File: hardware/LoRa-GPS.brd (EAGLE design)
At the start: 50.8 x 17.8 mm, 27 parts, among them J2 MF-CON-MICROUSB-RIGHT, U1 MCP1703-3302E/CB, Y1 CRYSTAL.ABS07

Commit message: lipo
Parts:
- added C10: 4.7uF, SparkFun-Capacitors:0603
- added C11: 10uF, SparkFun-Capacitors:EIA3216
- added D4: BLUE, SparkFun-LED:LED-0603
- added J8: (no value), SparkFun-Connectors:1X02_NO_SILK
- added R5: 2.0k, SparkFun-Resistors:0603
- added R9: 1k, SparkFun-Resistors:0603
- added U2: MCP73831, SparkFun-IC-Power:SOT23-5
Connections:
- new net CHARGE_STAT: R9.1, U2.1
- new net N$11: R5.1, U2.5
- new net N$8: D4.C, R9.2
- new net V_BATT: C11.+, U2.3
- new net V_USB: C10.1, D4.A, J8.2, U2.4
- net GND: now also C10.2, C11.-, J8.1, R5.2, U2.2
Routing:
- net VIN: track 13.1 -> 11.5 mm

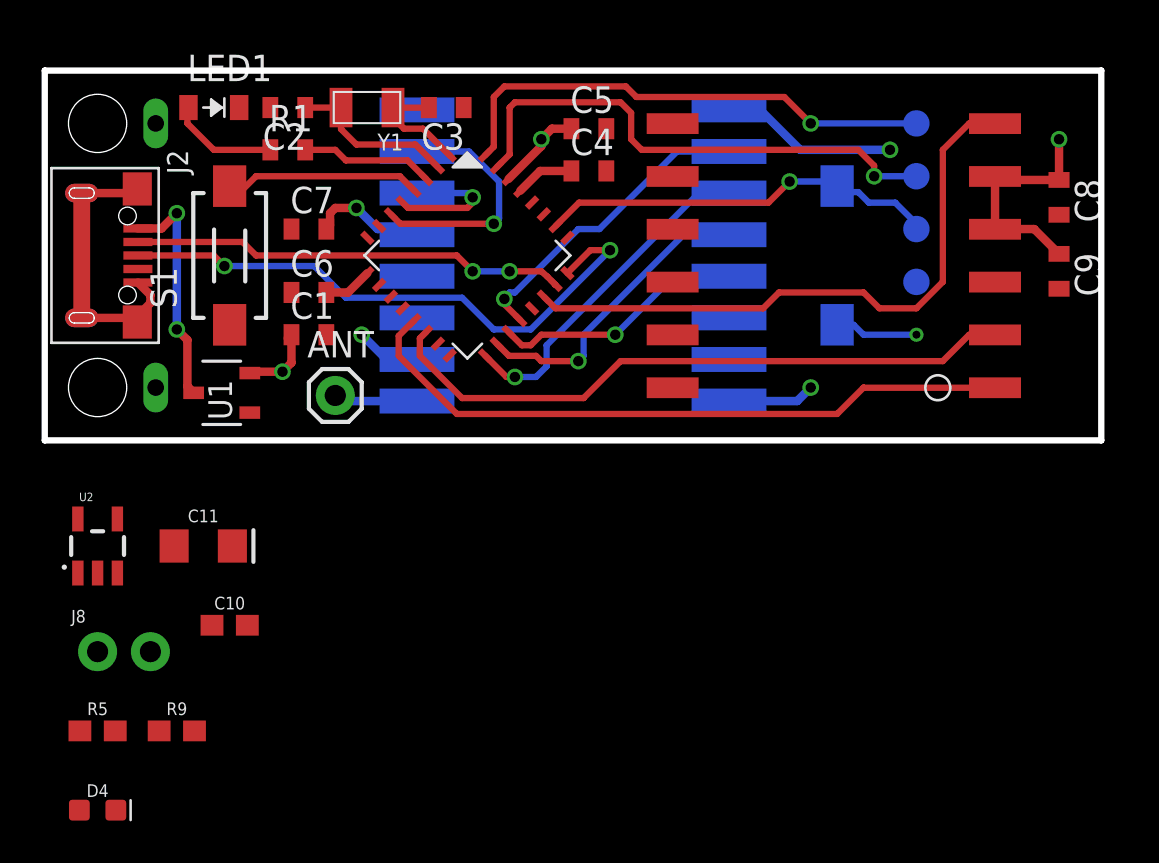
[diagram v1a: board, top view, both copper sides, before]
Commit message: remove DRC warnings
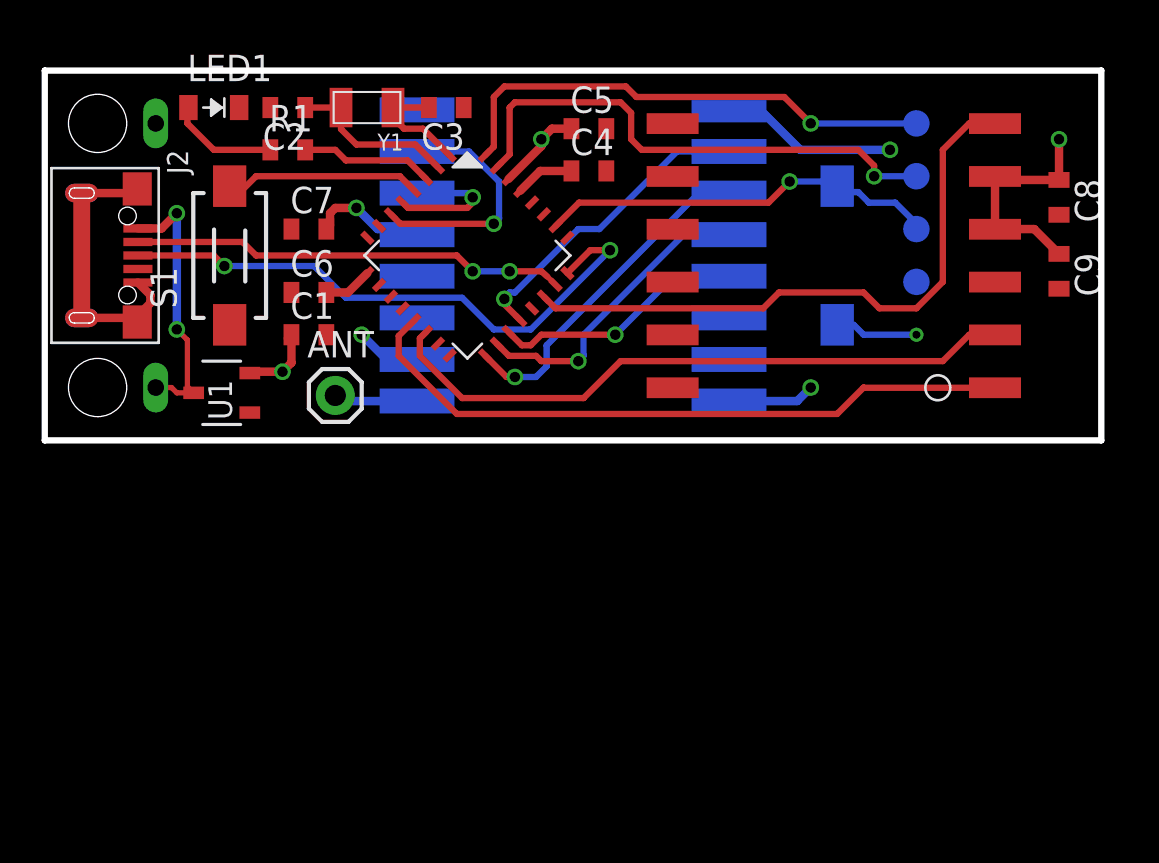
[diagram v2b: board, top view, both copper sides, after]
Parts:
- removed C10: 4.7uF, SparkFun-Capacitors:0603
- removed C11: 10uF, SparkFun-Capacitors:EIA3216
- removed D4: BLUE, SparkFun-LED:LED-0603
- removed J8: (no value), SparkFun-Connectors:1X02_NO_SILK
- removed R5: 2.0k, SparkFun-Resistors:0603
- removed R9: 1k, SparkFun-Resistors:0603
- removed U2: MCP73831, SparkFun-IC-Power:SOT23-5
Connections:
- removed net CHARGE_STAT: R9.1, U2.1
- removed net N$11: R5.1, U2.5
- removed net N$8: D4.C, R9.2
- removed net V_BATT: C11.+, U2.3
- removed net V_USB: C10.1, D4.A, J8.2, U2.4
- net GND: no longer C10.2, C11.-, J8.1, R5.2, U2.2
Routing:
- net VIN: track 11.5 -> 13.1 mm
- net N$3: track 9.04 -> 8.42 mm

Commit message: remove switch move TP's
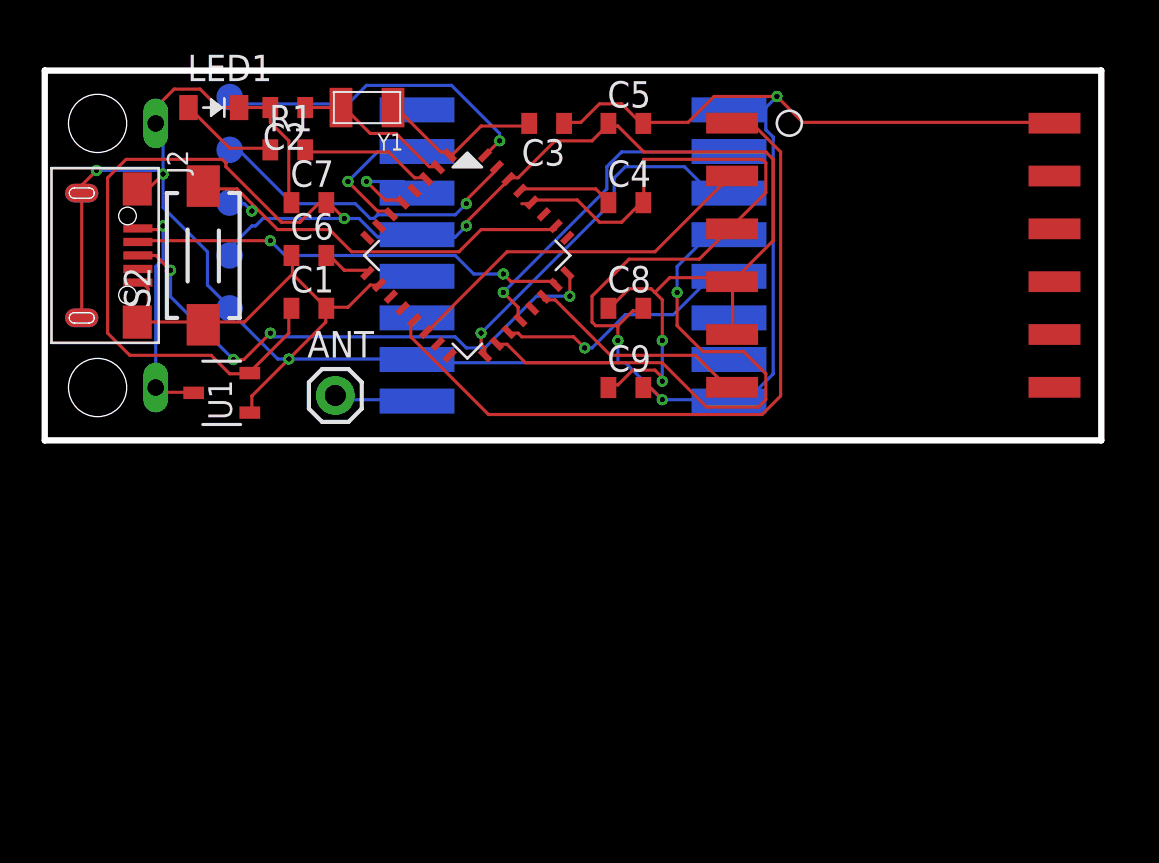
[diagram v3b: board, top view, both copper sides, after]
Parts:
- removed S1: DTSM-3, switch-tact:DTSM-3
- TP1: device SparkFun-Passives:TP_15TH -> SparkFun-Passives:PAD.03X.05
- moved TP1 33.0 mm to (8.89, 6.35), flipped to the bottom, turned to 180 degrees
- moved TP2 33.0 mm to (8.89, 8.89)
- moved TP3 33.0 mm to (8.89, 11.4)
- moved TP4 33.0 mm to (8.89, 14.0)
- moved TP5 33.0 mm to (8.89, 16.5)
- moved GPS 30.6 mm to (50.8, 19.1), turned to 180 degrees
- moved S2 30.5 mm to (7.62, 8.89), flipped to the top
- moved C9 21.6 mm to (27.9, 2.54), turned to 0 degrees
- moved C8 21.5 mm to (27.9, 6.35), turned to 0 degrees
- moved C3 4.89 mm to (24.1, 15.2)
- moved C4 2.34 mm to (27.9, 11.4)
- moved C5 1.80 mm to (27.9, 15.2)
- moved C6 1.78 mm to (12.7, 8.89)
- moved C1 1.27 mm to (12.7, 6.35)
- moved C7 1.27 mm to (12.7, 11.4)
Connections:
- removed net N$9: S1.2, SAMD21.4
- net GND: no longer S1.1
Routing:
- net GND: track 33.8 -> 164.7 mm, vias 3 -> 6
- net VCC: track 25.4 -> 87.2 mm
- net D21: track 30.0 -> 11.0 mm
- net RX: track 31.0 -> 17.8 mm
- net SCK: track 14.6 -> 26.8 mm
- net N$9: track 10.1 -> 0.00 mm
- net SWCLK: track 25.3 -> 15.4 mm
- net SWDIO: track 24.3 -> 15.9 mm
- net D18: track 11.8 -> 6.64 mm
- net TX: track 32.4 -> 35.3 mm
- net VIN: track 13.1 -> 11.2 mm, vias 2 -> 1
- net D17: track 6.59 -> 4.81 mm
- net N$5: track 2.85 -> 4.57 mm
- net D+: track 28.3 -> 26.6 mm, vias 2 -> 4
- net MOSI: track 16.4 -> 17.5 mm
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- added copper zone on layer 16, net GND
- removed copper zone on layer 16, net VCC

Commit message: tidy
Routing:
- net GND: track 164.7 -> 164.0 mm
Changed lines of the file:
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@@
 <drawing>
 <settings>
-<setting alwaysvectorfont="yes"/>
+<setting alwaysvectorfont="no"/>
 <setting keepoldvectorfont="yes"/>
 <setting verticaltext="up"/>
@@
 <layer number="23" name="tOrigins" color="15" fill="1" visible="yes" active="yes"/>
 <layer number="24" name="bOrigins" color="15" fill="1" visible="yes" active="yes"/>
-<layer number="25" name="tNames" color="7" fill="1" visible="yes" active="yes"/>
-<layer number="26" name="bNames" color="7" fill="1" visible="yes" active="yes"/>
+<layer number="25" name="tNames" color="7" fill="1" visible="no" active="yes"/>
+<layer number="26" name="bNames" color="7" fill="1" visible="no" active="yes"/>
 <layer number="27" name="tValues" color="7" fill="1" visible="no" active="yes"/>
 <layer number="28" name="bValues" color="7" fill="1" visible="no" active="yes"/>
@@
 <layer number="37" name="tTest" color="7" fill="1" visible="no" active="yes"/>
 <layer number="38" name="bTest" color="7" fill="1" visible="no" active="yes"/>
-<layer number="39" name="tKeepout" color="4" fill="11" visible="yes" active="yes"/>
-<layer number="40" name="bKeepout" color="1" fill="11" visible="yes" active="yes"/>
-<layer number="41" name="tRestrict" color="4" fill="10" visible="yes" active="yes"/>
-<layer number="42" name="bRestrict" color="1" fill="10" visible="yes" active="yes"/>
+<layer number="39" name="tKeepout" color="4" fill="11" visible="no" active="yes"/>
+<layer number="40" name="bKeepout" color="1" fill="11" visible="no" active="yes"/>
+<layer number="41" name="tRestrict" color="4" fill="10" visible="no" active="yes"/>
+<layer number="42" name="bRestrict" color="1" fill="10" visible="no" active="yes"/>
 <layer number="43" name="vRestrict" color="2" fill="10" visible="no" active="yes"/>
 <layer number="44" name="Drills" color="7" fill="1" visible="no" active="yes"/>
-<layer number="45" name="Holes" color="7" fill="1" visible="no" active="yes"/>
+<layer number="45" name="Holes" color="7" fill="1" visible="yes" active="yes"/>
 <layer number="46" name="Milling" color="3" fill="1" visible="no" active="yes"/>
 <layer number="47" name="Measures" color="7" fill="1" visible="no" active="yes"/>
@@
 <layer number="50" name="dxf" color="7" fill="1" visible="no" active="no"/>
 <layer number="51" name="tDocu" color="6" fill="1" visible="yes" active="yes"/>
-<layer number="52" name="bDocu" color="7" fill="1" visible="yes" active="yes"/>
+<layer number="52" name="bDocu" color="7" fill="1" visible="no" active="yes"/>
 <layer number="53" name="tGND_GNDA" color="7" fill="9" visible="no" active="no"/>
 <layer number="54" name="bGND_GNDA" color="1" fill="9" visible="no" active="no"/>
@@
 <contactref element="C1" pad="2"/>
 <contactref element="C4" pad="2"/>
-<contactref element="SAMD21" pad="28"/>
 <contactref element="C5" pad="2"/>
 <contactref element="J2" pad="5"/>
@@
 <wire x1="27.7368" y1="10.4902" x2="26.67" y2="10.4902" width="0.1524" layer="1"/>
 <wire x1="28.6258" y1="11.3792" x2="27.7368" y2="10.4902" width="0.1524" layer="1"/>
-<wire x1="23.4696" y1="11.557" x2="23.43126875" y2="11.435584375" width="0.1524" layer="1"/>
 <wire x1="28.6258" y1="11.3792" x2="28.7782" y2="11.43" width="0.1524" layer="1"/>
 <wire x1="28.8036" y1="11.557" x2="28.8036" y2="13.5128" width="0.1524" layer="1"/>
@@
 <wire x1="9.779" y1="1.4224" x2="9.859" y2="1.336" width="0.1524" layer="1"/>
 <wire x1="7.6454" y1="5.5118" x2="7.62" y2="5.555" width="0.1524" layer="1"/>
-<wire x1="22.9362" y1="11.3792" x2="23.2918" y2="11.3792" width="0.1524" layer="1"/>
-<wire x1="23.2918" y1="11.3792" x2="23.43126875" y2="11.435584375" width="0.1524" layer="1"/>
 <wire x1="16.1798" y1="7.6454" x2="16.07735625" y2="7.475784375" width="0.1524" layer="1"/>
 <wire x1="34.671" y1="11.9126" x2="33.0708" y2="10.3124" width="0.1524" layer="1"/>
@@
 <vertex x="50.8" y="17.78"/>
 </polygon>
+<contactref element="SAMD21" pad="28"/>
 </signal>
 <signal name="VCC">
 <contactref element="C1" pad="1"/>
 <contactref element="U1" pad="2"/>
-<contactref element="SAMD21" pad="30"/>
 <contactref element="C5" pad="1"/>
 <contactref element="RADIO" pad="B4"/>
@@
 <wire x1="26.3144" y1="14.4018" x2="24.5364" y2="14.4018" width="0.1524" layer="1"/>
 <wire x1="27.0256" y1="15.113" x2="26.3144" y2="14.4018" width="0.1524" layer="1"/>
-<wire x1="22.4028" y1="12.6238" x2="22.299896875" y2="12.566953125" width="0.1524" layer="1"/>
 <wire x1="27.0256" y1="15.113" x2="27.1018" y2="15.24" width="0.1524" layer="1"/>
 <wire x1="27.559" y1="2.667" x2="27.2034" y2="2.667" width="0.1524" layer="1"/>
@@
 <wire x1="19.7358" y1="9.779" x2="20.2692" y2="10.3124" width="0.1524" layer="16"/>
 <wire x1="17.9578" y1="9.779" x2="19.7358" y2="9.779" width="0.1524" layer="16"/>
-<wire x1="22.225" y1="12.446" x2="22.299896875" y2="12.566953125" width="0.1524" layer="1"/>
 <wire x1="17.9578" y1="9.779" x2="17.9" y2="9.89" width="0.1524" layer="16"/>
 <via x="29.6926" y="2.8448" extent="1-16" drill="0.254"/>
@@
 <via x="14.4018" y="10.668" extent="1-16" drill="0.254"/>
 <via x="20.2692" y="10.3124" extent="1-16" drill="0.254"/>
-</signal>
-<signal name="N$5">
-<contactref element="SAMD21" pad="29"/>
-<contactref element="C4" pad="1"/>
-<wire x1="26.4922" y1="12.0904" x2="22.9362" y2="12.0904" width="0.1524" layer="1"/>
-<wire x1="27.0256" y1="11.557" x2="26.4922" y2="12.0904" width="0.1524" layer="1"/>
-<wire x1="22.9362" y1="12.0904" x2="22.865584375" y2="12.00126875" width="0.1524" layer="1"/>
-<wire x1="27.0256" y1="11.557" x2="27.1018" y2="11.43" width="0.1524" layer="1"/>
+<contactref element="SAMD21" pad="30"/>
+<wire x1="22.4028" y1="12.6238" x2="22.299896875" y2="12.566953125" width="0.1524" layer="1"/>
+<wire x1="22.225" y1="12.446" x2="22.299896875" y2="12.566953125" width="0.1524" layer="1"/>
 </signal>
 <signal name="VIN">
@@
 <signal name="N$10">
 </signal>
+<signal name="N$5">
+<contactref element="SAMD21" pad="29"/>
+<contactref element="C4" pad="1"/>
+<wire x1="22.865584375" y1="12.00126875" x2="23.564315625" y2="12.7" width="0.1524" layer="1"/>
+<wire x1="25.8318" y1="12.7" x2="27.1018" y2="11.43" width="0.1524" layer="1"/>
+<wire x1="23.564315625" y1="12.7" x2="25.8318" y2="12.7" width="0.1524" layer="1"/>
+</signal>
 </signals>

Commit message: tinker
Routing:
- net GND: track 164.0 -> 36.2 mm, vias 6 -> 5

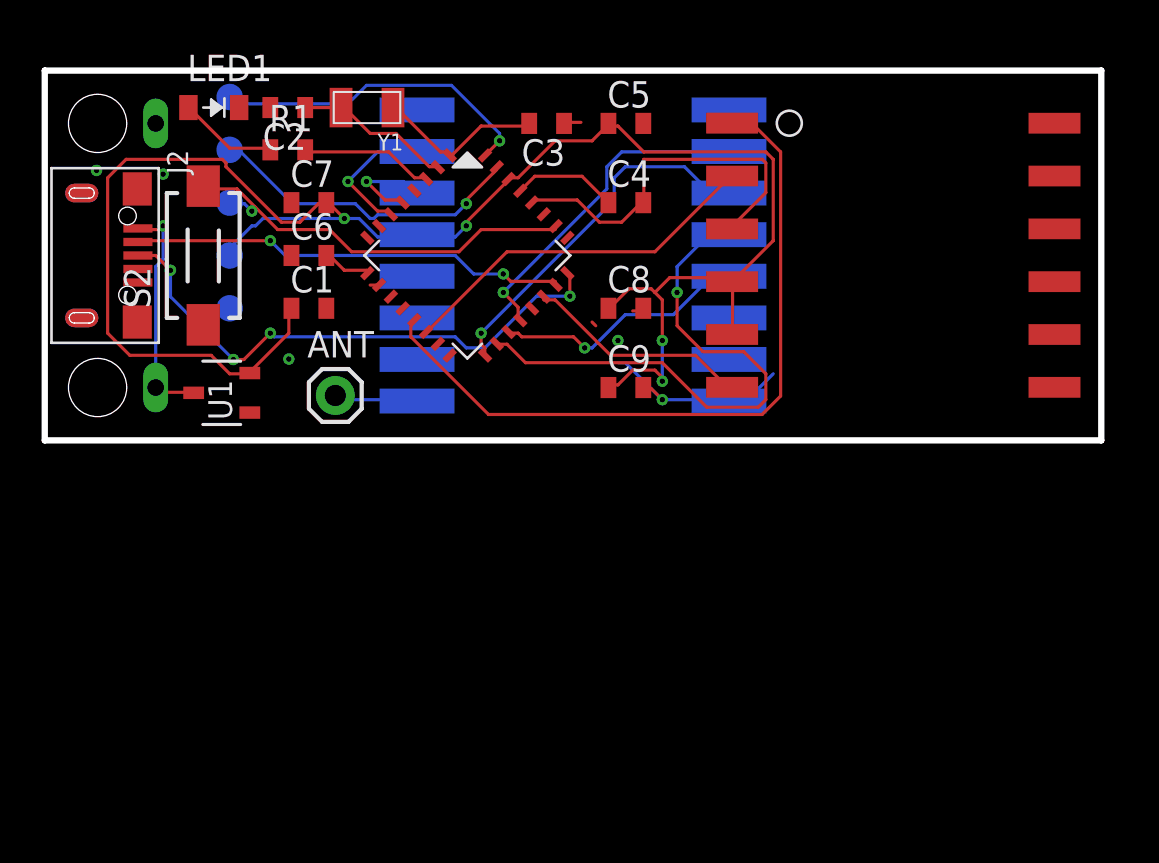
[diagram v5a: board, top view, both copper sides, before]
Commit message: RF and GPS underside
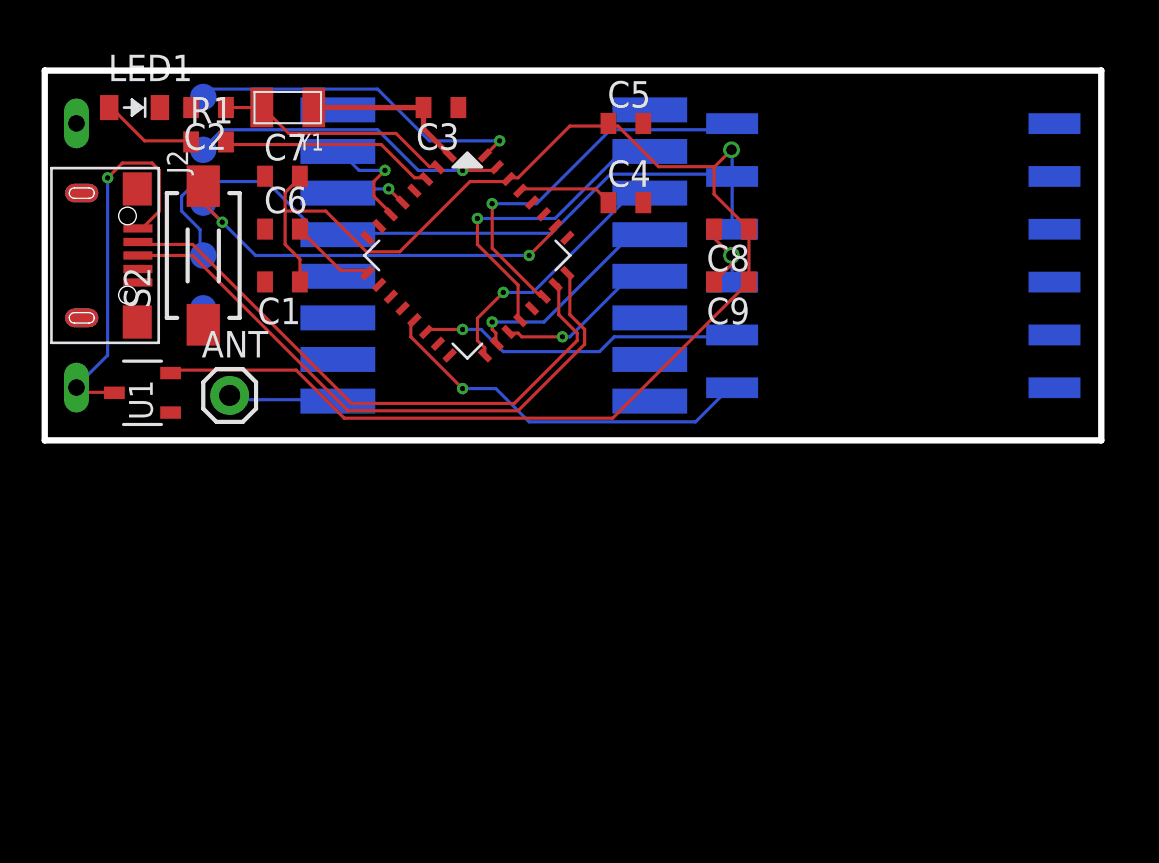
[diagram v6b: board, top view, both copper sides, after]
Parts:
- moved GPS 20.3 mm to (50.8, -1.27), flipped to the bottom, turned to 0 degrees
- moved C9 7.18 mm to (33.0, 7.62), turned to 180 degrees
- moved C8 6.35 mm to (33.0, 10.2), turned to 180 degrees
- moved C3 5.14 mm to (19.1, 16.0)
- moved ANT 5.08 mm to (8.89, 2.16)
- moved R1 3.83 mm to (7.87, 14.4)
- moved LED1 3.81 mm to (4.32, 16.0)
- moved U1 3.81 mm to (4.70, 2.29)
- moved Y1 3.81 mm to (11.7, 16.0)
- moved C2 3.81 mm to (7.87, 16.0)
- moved JP1 3.81 mm to (1.52, 2.54)
- moved JP2 3.81 mm to (1.52, 15.2)
- moved RADIO 3.81 mm to (21.6, 8.89)
- moved C1 1.80 mm to (11.4, 7.62), turned to 180 degrees
- moved C6 1.80 mm to (11.4, 10.2)
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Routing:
- net GND: track 36.2 -> 4.54 mm, vias 5 -> 1
- net VCC: track 87.2 -> 105.8 mm, vias 4 -> 1
- net TX: track 35.3 -> 18.7 mm, vias 0 -> 1
- net SCK: track 26.8 -> 10.4 mm
- net VIN: track 11.2 -> 18.9 mm
- net D-: track 21.1 -> 28.8 mm, vias 2 -> 0
- net D21: track 11.0 -> 18.7 mm, vias 0 -> 1
- net MOSI: track 17.5 -> 12.7 mm
- net SS: track 12.4 -> 8.08 mm
- net N$6: track 6.41 -> 10.5 mm
- net N$2: track 7.57 -> 11.4 mm
- net D+: track 26.6 -> 29.7 mm, vias 4 -> 0
- net RX: track 17.8 -> 15.5 mm, vias 0 -> 1
- net N$1: track 2.37 -> 4.18 mm
- net D17: track 4.81 -> 3.46 mm
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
